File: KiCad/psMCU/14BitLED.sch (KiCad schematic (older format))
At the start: 28 parts

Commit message: Started ClockTest PCB
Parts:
- removed D? (x6): LED, Diode_SMD:D_0603_1608Metric, symbol Device:LED_Small
- removed R? (x11): rled, Resistor_SMD:R_0603_1608Metric, symbol Device:R_Small
- added D? (x6): LED, Diode_SMD:D_0603_1608Metric, symbol Device:LED_Small
- added R? (x11): rled, Resistor_SMD:R_0603_1608Metric, symbol Device:R_Small
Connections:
- net GND: now also D?.1 (K), D?.1 (K), D?.1 (K), D?.1 (K), D?.1 (K), D?.1 (K)
- net VAL0: now also R?.2
- net VAL1: now also R?.2
- net VAL10: now also R?.2
- net VAL11: now also R?.2
- net VAL12: now also R?.2
- net VAL13: now also R?.2
- net VAL2: now also R?.2
- net VAL5: now also R?.2
- net VAL6: now also R?.2
- net VAL7: now also R?.2
- net VAL8: now also R?.2
- net at D?.2 (A): now also R?.1 (x6)
- net at R?.1: now also D?.2 (A)
- new net: D?.2 (A), R?.1 (x5)

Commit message: First Schematic Draft done.
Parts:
- D104, D105, D106, D107, D108, D109, D110, D111, D112, D113, D114, D115, D116, D117: renamed from D?; footprint Diode_SMD:D_0603_1608Metric -> NoRef_Footprints:D_0603_1608Metric_NoRef
- R109, R110, R111, R112, R113, R114, R115, R116, R117, R118, R119, R120, R121, R122: renamed from R?; footprint Resistor_SMD:R_0603_1608Metric -> NoRef_Footprints:R_0603_1608Metric

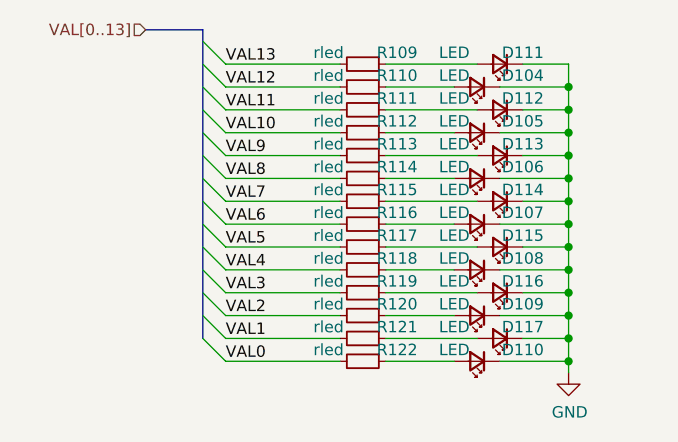
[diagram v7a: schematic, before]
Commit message: Cleanup, ready for specific component values.
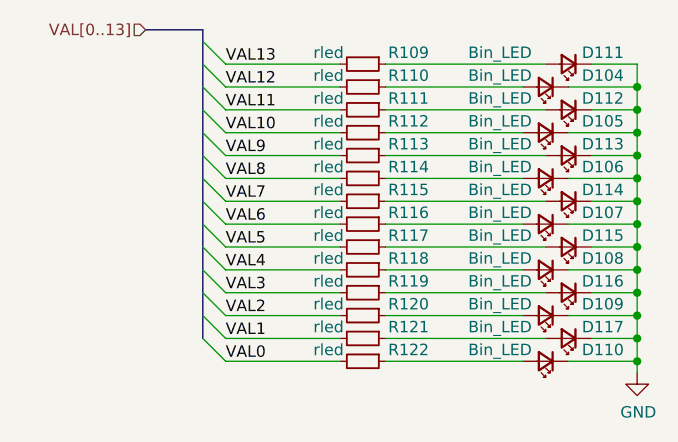
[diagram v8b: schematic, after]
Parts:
- D104, D105, D106, D107, D108, D109, D110, D111, D112, D113, D114, D115, D116, D117: value LED -> Bin_LED
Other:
- moved on the sheet: D104, D105, D106, D107, D108, D109, D110, D111, D112, D113, D114, D115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
